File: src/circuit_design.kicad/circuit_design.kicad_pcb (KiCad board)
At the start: 2 copper layers, 198.8 x 170.8 mm, 185 parts, among them J1 CONN_BAT, Q1 BT134-600E, Q2 BT134-600E, Q3 BT134-600E, Q4 BT134-600E, U1 К176ИЕ12, U10 К155ЛА4, U11 К155ЛИ1, U12 К155ЛА1, U13 К155ИЕ5, U14 К155ЛЛ1, U15 К155ЛН1, U16 К155ЛИ1, U17 К155ТВ15, U18 К155ИЕ5, U19 К155ЛП5, U2 К155ЛП10, U20 К155ИВ1, U21 К155ИД7, U22 К155ИД4, U23 К155ЛН1, U24 К155ЛП10, U25 MOC3062M, U26 MOC3062M, U27 MOC3062M, U28 MOC3062M, U29 LM7806_TO220, U3 К155ЛЕ3, U30 SC6038, U31 К155ЛЕ1, U32 К155ЛН1, U33 К155ЛИ1, U34 К155ЛА4, U35 К155ТВ15, U36 К155ТЛ2, U37 4020, U38 LM7806_TO220, U39 К155ЛН1, U4 К155ЛН1, U5 К155ЛИ1, U6 К155ЛЛ1, U7 4020, U8 ICL7660, U9 К155ИЕ5, Y1 32768

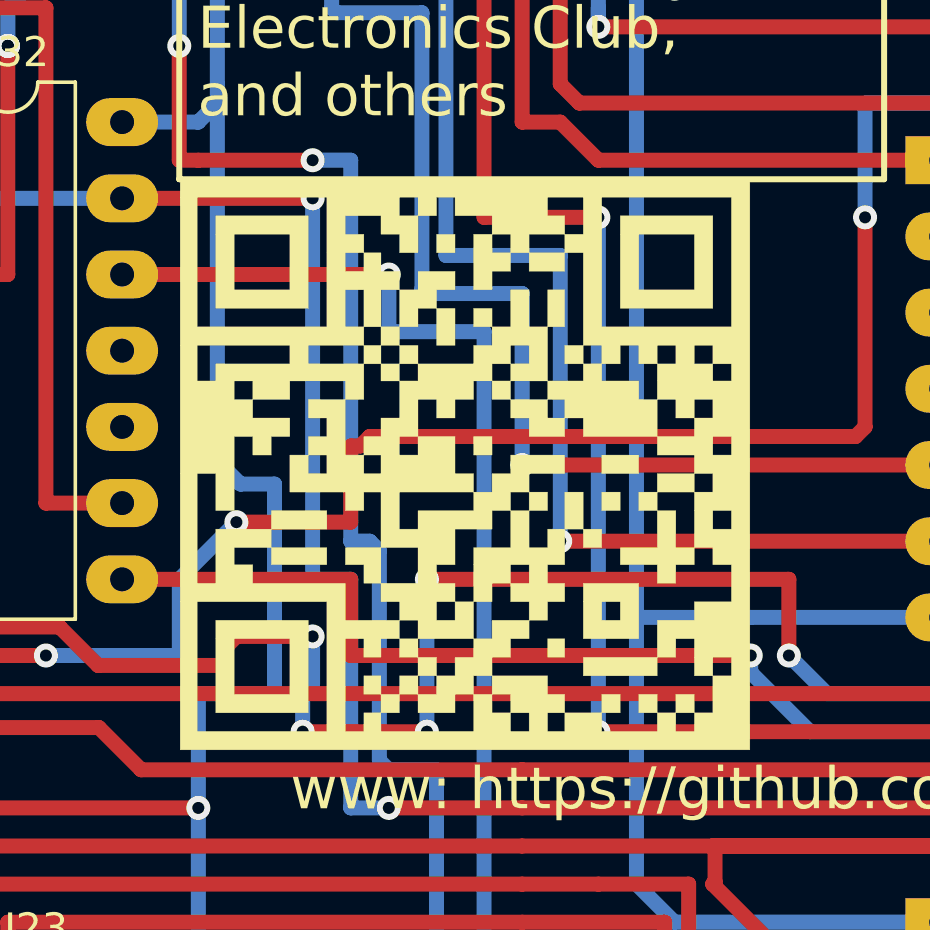
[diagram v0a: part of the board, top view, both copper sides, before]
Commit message: The PCB layout was updated from the schematic.
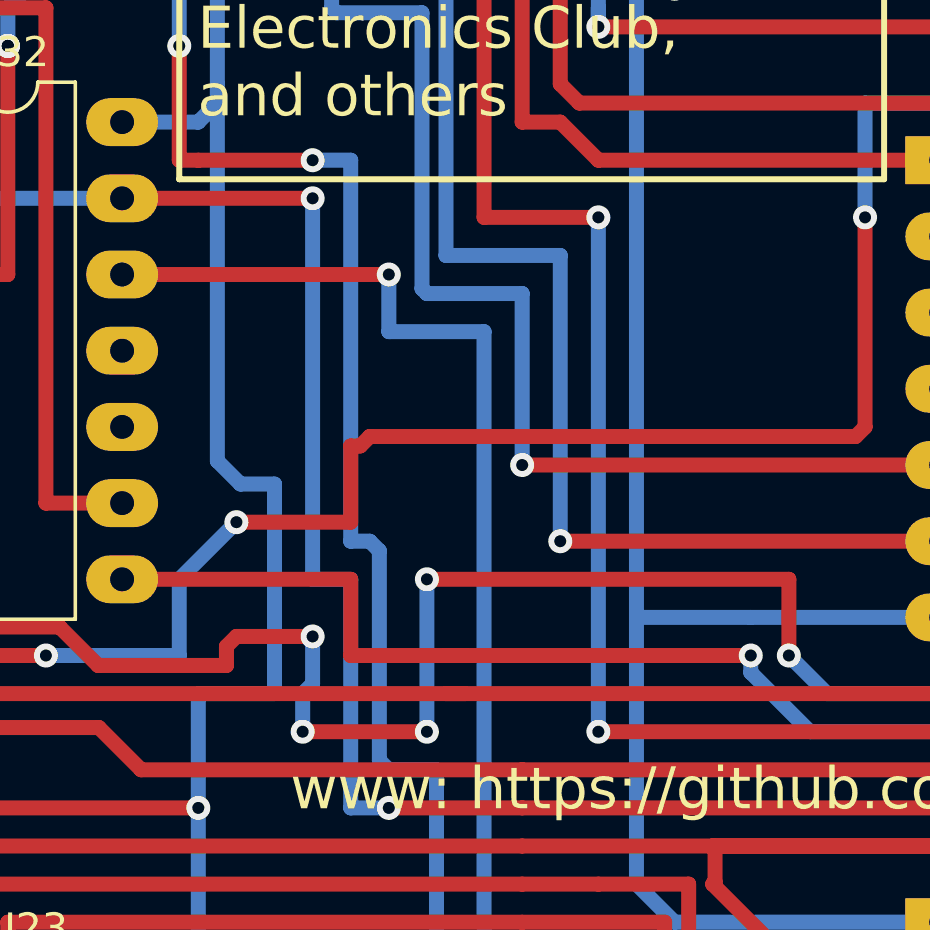
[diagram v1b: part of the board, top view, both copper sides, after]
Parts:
- removed the G*** at (137.8, 99.1)

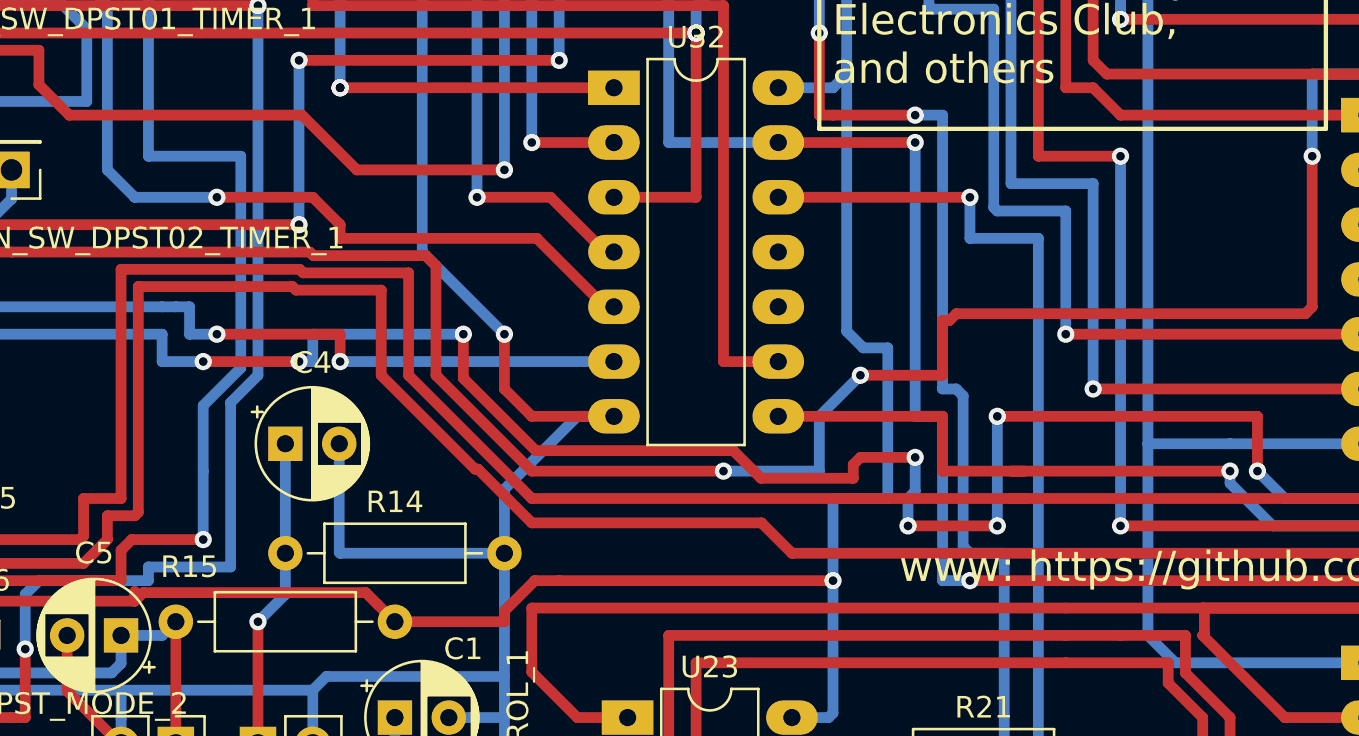
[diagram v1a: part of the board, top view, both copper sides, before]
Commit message: 01. The unnecessary element was removed 02. The QR code was added
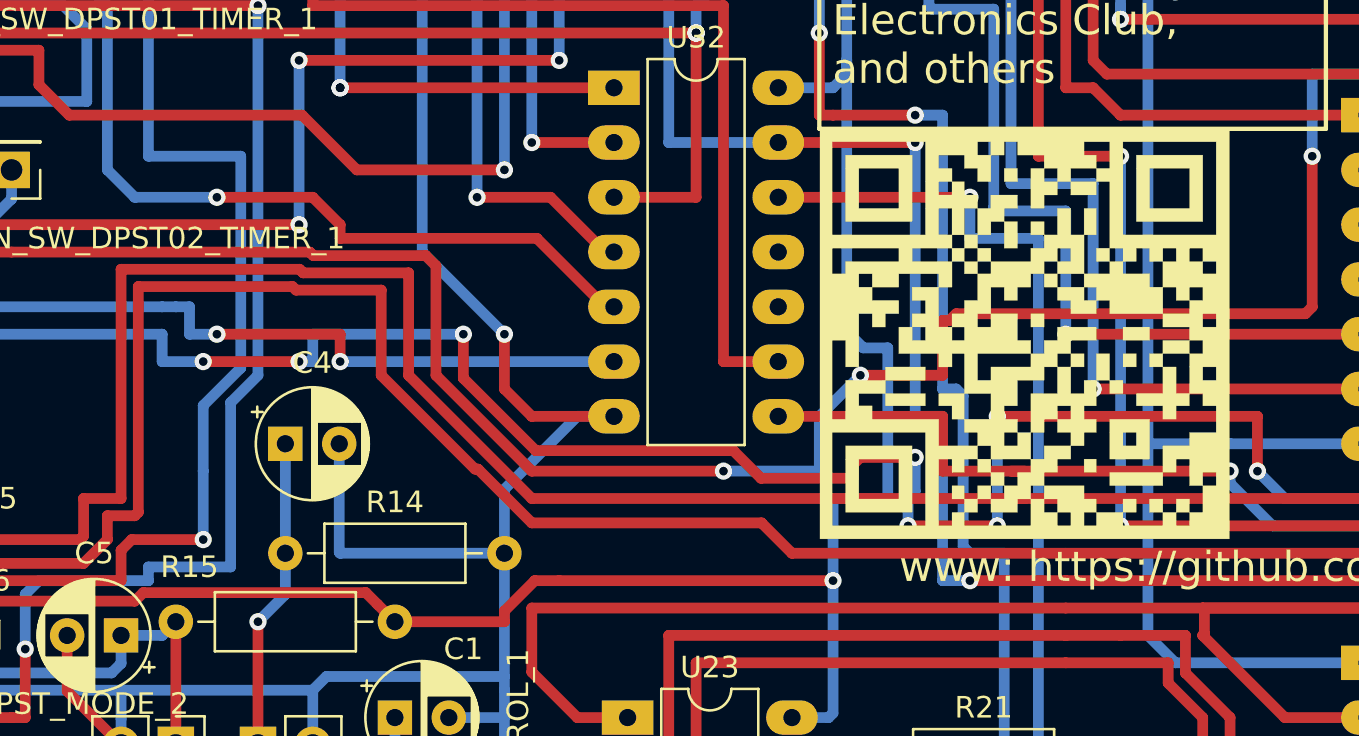
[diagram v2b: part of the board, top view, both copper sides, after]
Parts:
- added G***: LOGO, circuit_design:qrcode, F.Cu at (137.8, 99.1)

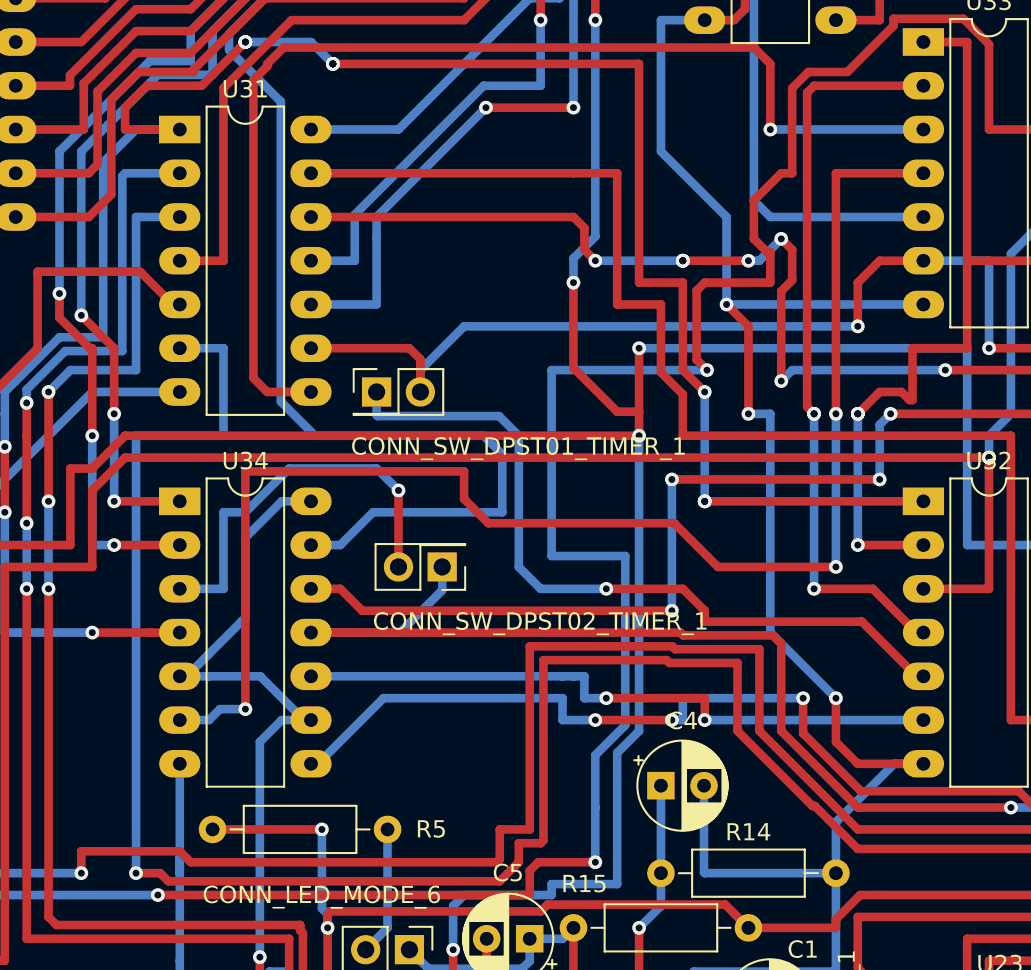
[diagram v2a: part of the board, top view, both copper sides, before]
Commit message: The timer reset logic was updated. Now it is resetting not by the start button/external signal but on enabed.
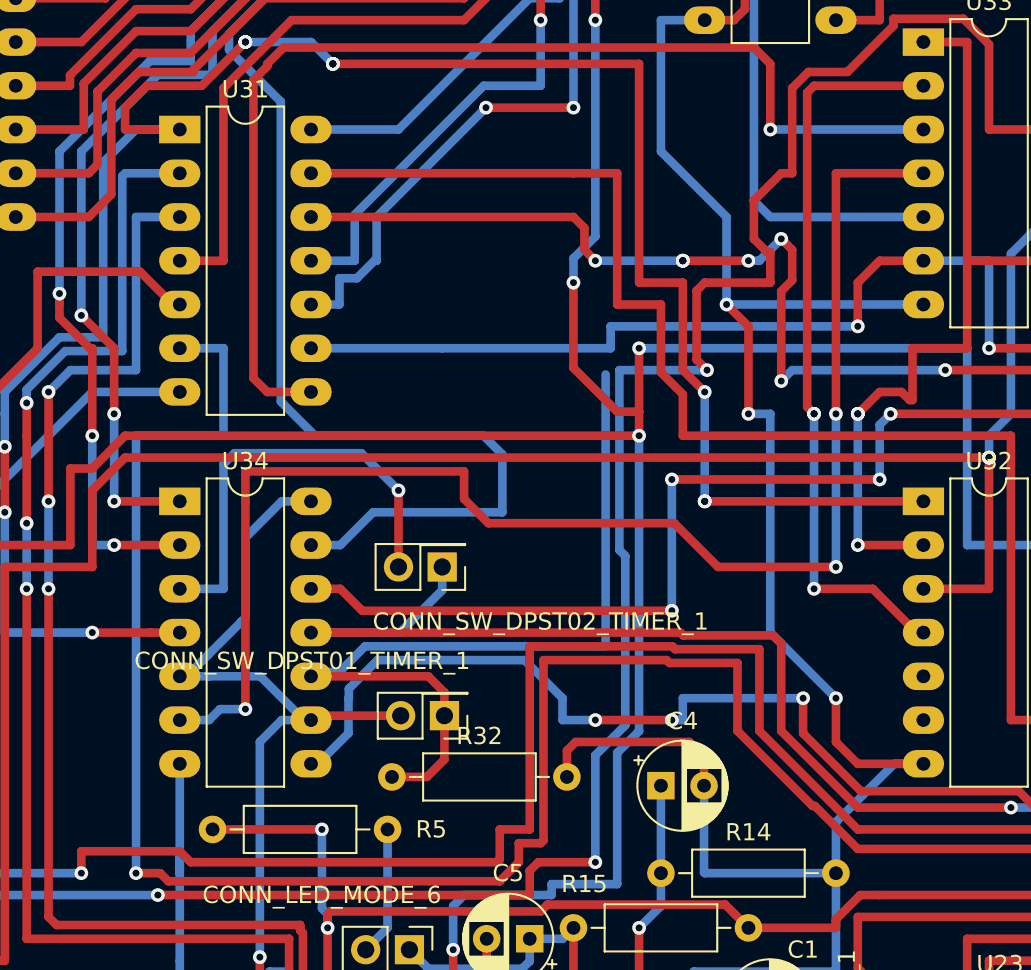
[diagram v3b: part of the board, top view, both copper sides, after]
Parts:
- added R32: 1 KOhm, Resistor_THT:R_Axial_DIN0207_L6.3mm_D2.5mm_P10.16mm_Horizontal, F.Cu at (87.9, 103.6)
- moved CONN_SW_DPST01_TIMER_1 19.2 mm to (90.9, 100.1), turned to 180 degrees
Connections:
- CONN_SW_DPST01_TIMER_1 pad 2: Net-(CONN_SW_DPST01_TIMER_1-Pad2) -> PWR_ALW
- U14 pad 9: Net-(CONN_SW_DPST01_TIMER_1-Pad2) -> Net-(U14-Pad9)
- U31 pad 9: Net-(CONN_SW_DPST01_TIMER_1-Pad2) -> Net-(U14-Pad9)
- U32 pad 5: Net-(CONN_SW_DPST01_TIMER_1-Pad1) -> (no net)
- U32 pad 6: Net-(U32-Pad6) -> (no net)
- U33 pad 6: Net-(CONN_SW_DPST01_TIMER_1-Pad2) -> Net-(U14-Pad9)
- U34 pad 10: Net-(U32-Pad6) -> Net-(CONN_SW_DPST01_TIMER_1-Pad1)
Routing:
- net Net-(CONN_SW_DPST01_TIMER_1-Pad2): track 203.0 -> 0.00 mm, vias 8 -> 0
- net Net-(U14-Pad9): track 0.00 -> 199.8 mm, vias 0 -> 8
- net Net-(U32-Pad6): track 38.1 -> 0.00 mm, vias 2 -> 0
- net GND: track 1965.1 -> 1976.9 mm
- net CLK_SEC: track 209.1 -> 201.1 mm
- net PWR_ALW: track 477.5 -> 482.8 mm
- net Net-(CONN_SW_DPST01_TIMER_1-Pad1): track 44.2 -> 49.1 mm, vias 1 -> 0
- net Net-(U34-Pad8): track 128.1 -> 131.4 mm
- net Net-(CONN_SW_DPST02_TIMER_1-Pad2): track 23.2 -> 25.5 mm
- net Net-(U31-Pad10): track 45.1 -> 44.5 mm

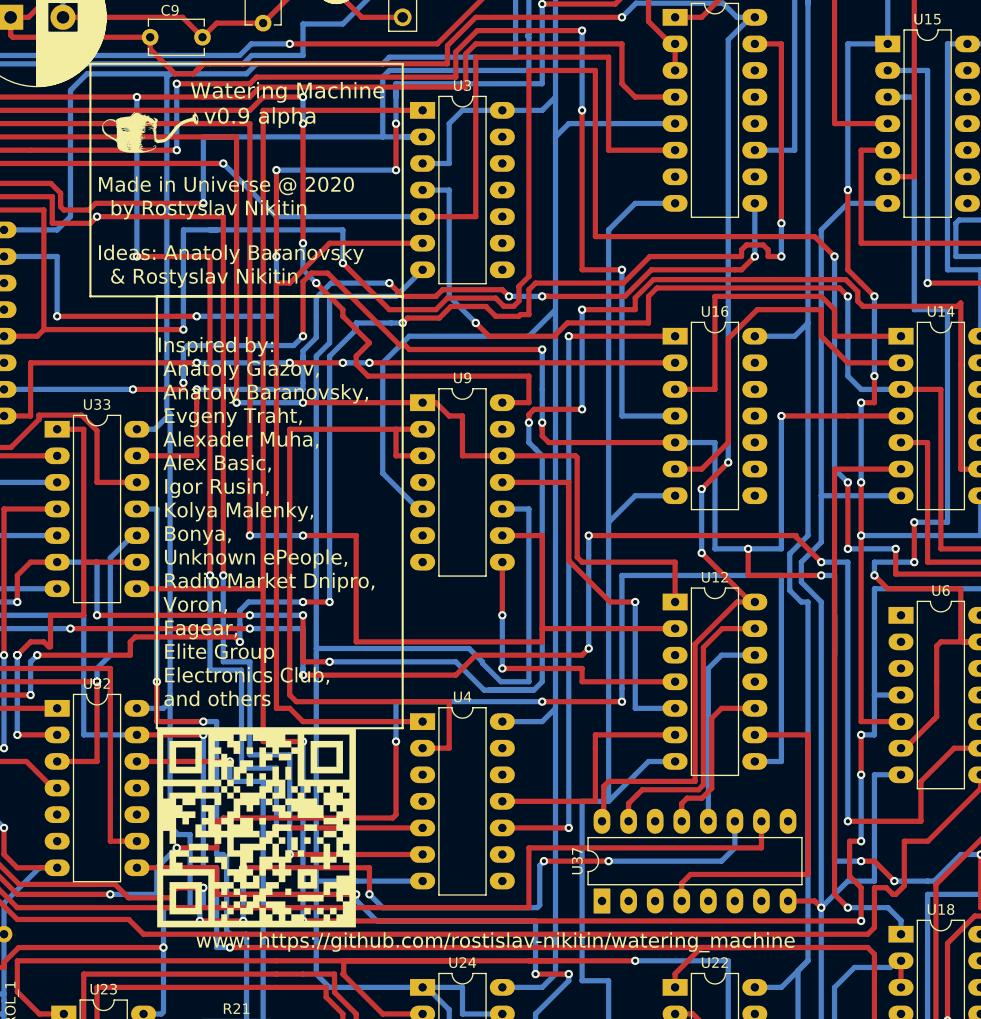
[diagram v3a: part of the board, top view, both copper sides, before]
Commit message: PCB layout was updated
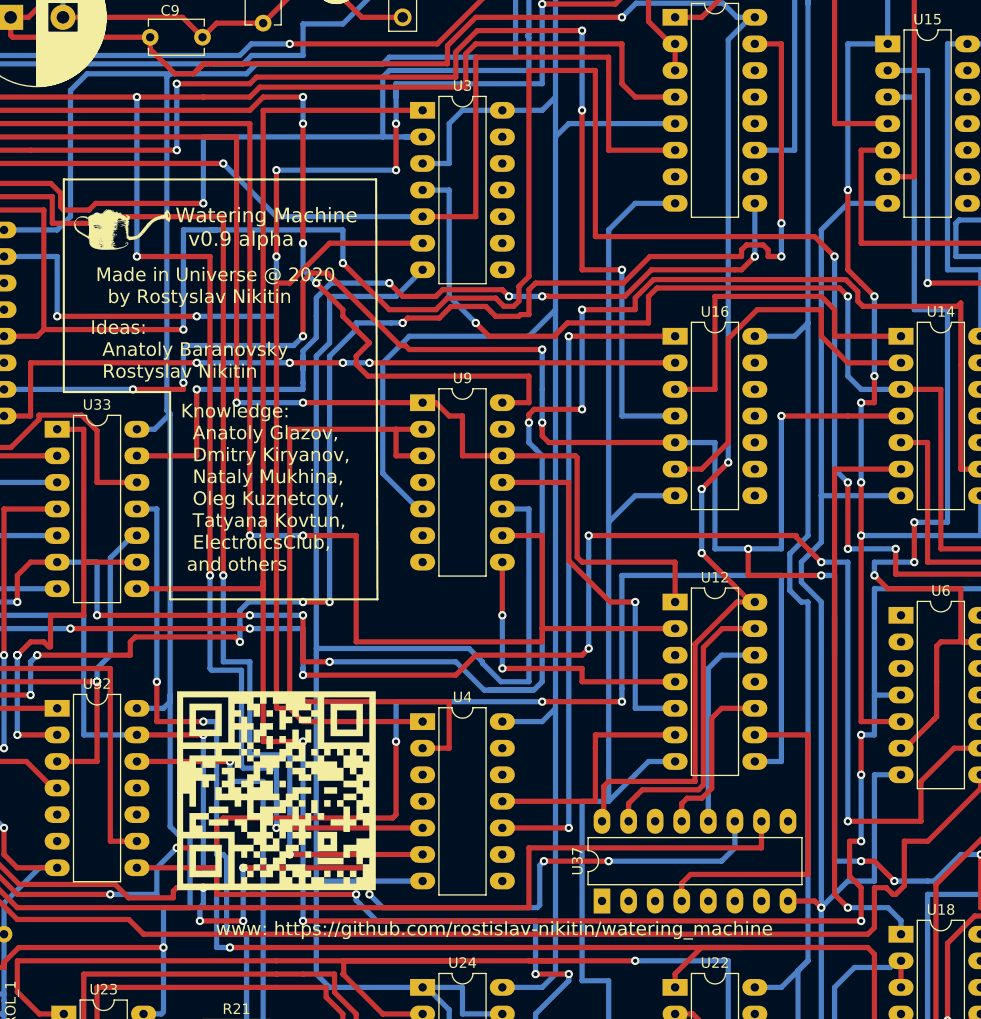
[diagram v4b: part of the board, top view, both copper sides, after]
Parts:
- moved G*** 9.65 mm to (125.0, 41.7)
- moved G*** 4.03 mm to (139.7, 95.5)
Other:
- board text added: "Ideas: Anatoly Baranovsky Rostyslav Nikitin"
- board text added: "Knowledge: Anatoly Glazov, Dmitry Kiryanov, Nataly Mukhina, Oleg Kuznetcov, Tatyana Kovtun, ElectroicsClub, and others"
- board text removed: "Ideas: Anatoly Baranovsky & Rostyslav Nikitin"
- board text removed: "Inspired by: Anatoly Glazov, Anatoly Baranovsky, Evgeny Traht, Alexader Muha, Alex Basic, Igor Rusin, Kolya Malenky, Bonya, Unknown ePeople, Radio Market Dnipro, Voron, Fagear, Elite Group Electronics Club, and others"
